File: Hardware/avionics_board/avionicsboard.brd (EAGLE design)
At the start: 39.1 x 105 mm, 17 parts, among them IC1 788TV, J1 Breakout1, J2 Breakout2, M1 SERVO, M2 SERVO

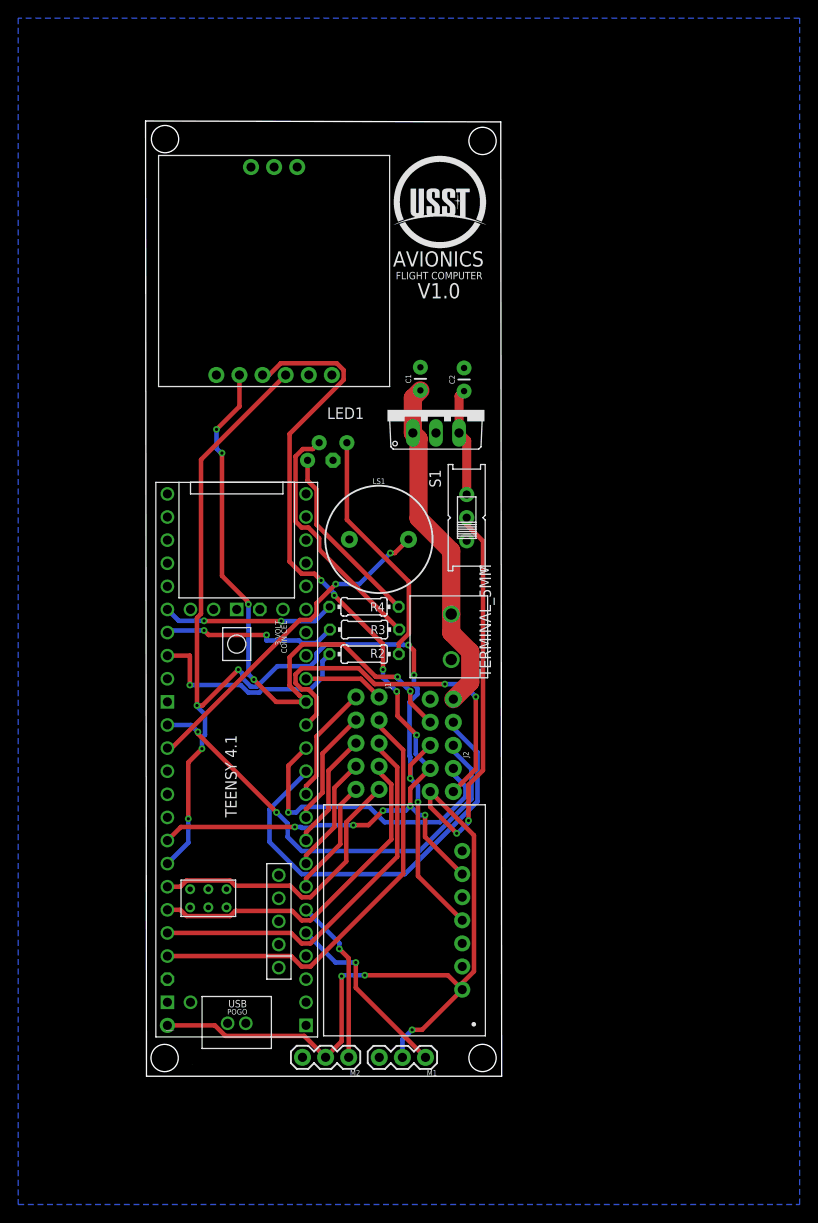
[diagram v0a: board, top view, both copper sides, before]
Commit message: Combined Avionics board and BMI088 board into on PCB named Combined Board, added space for plunger to fit around the combined board. Changed Avionics board to include a diode and power switch.
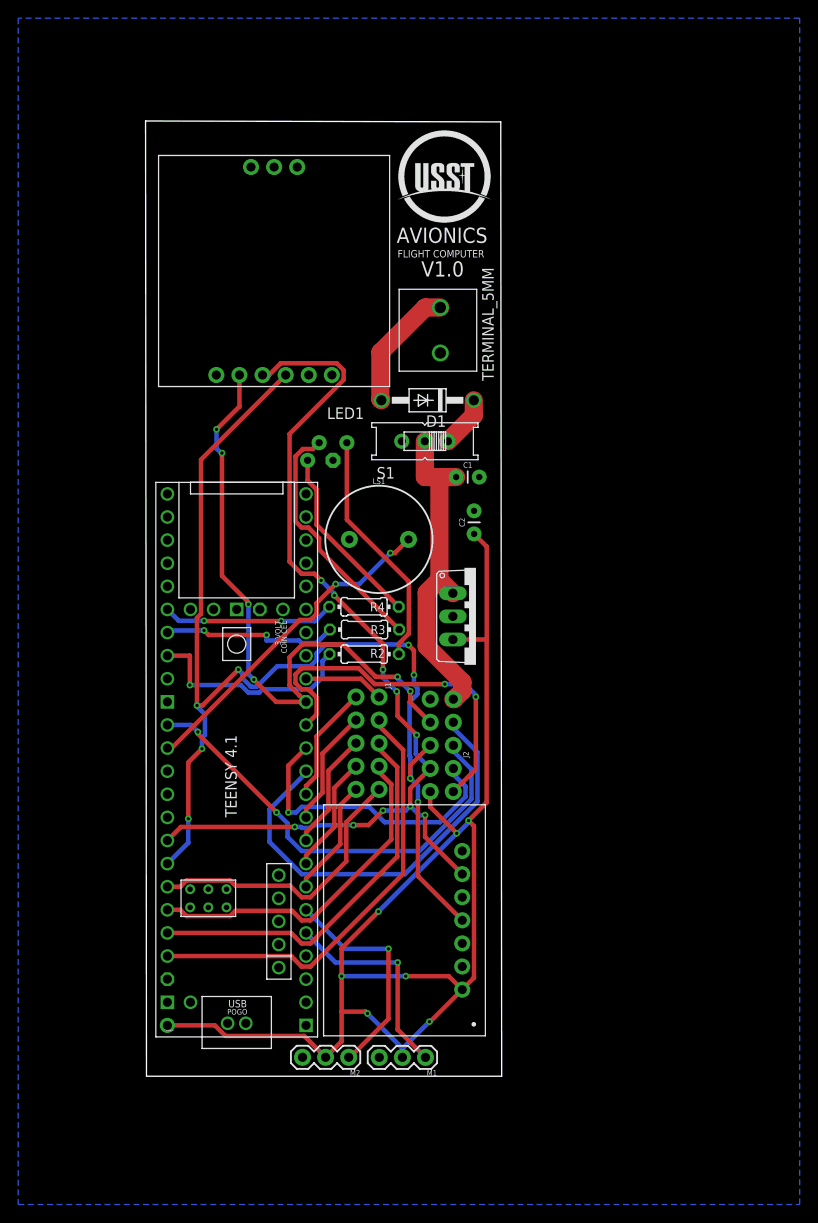
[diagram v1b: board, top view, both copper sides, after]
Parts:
- added D1: 1N4004, diode:DO41-10
- moved TERMINAL 33.7 mm to (27.3, 86.5)
- moved IC1 23.1 mm to (36.2, 50.5), turned to 270 degrees
- moved C2 15.7 mm to (36.0, 60.9)
- moved C1 12.0 mm to (35.3, 65.9), turned to 0 degrees
- moved S1 9.58 mm to (30.6, 69.8), turned to 180 degrees
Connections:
- removed net N$1: C2.1, IC1.3, S1.S
- new net N$5: D1.A, TERMINAL.1
- new net N$6: D1.C, S1.O
- net 12V: now also S1.P; no longer TERMINAL.1
- net 5V: now also C2.1, IC1.3; no longer S1.P
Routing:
- net 5V: track 120.1 -> 146.8 mm, vias 5 -> 7
- net N$5: track 0.00 -> 13.9 mm
- net N$1: track 11.9 -> 0.00 mm
- net TVCY: track 18.2 -> 24.7 mm
- net N$6: track 0.00 -> 5.68 mm
- net TVCX: track 20.4 -> 23.1 mm
- net 12V: track 37.7 -> 36.5 mm
